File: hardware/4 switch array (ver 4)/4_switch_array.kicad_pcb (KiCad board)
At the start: 2 copper layers, 45.5 x 48.5 mm, 24 parts, among them J1 Conn_01x04, J2 Conn_01x04, J3 Conn_01x02, J4 Conn_01x02, J5 Conn_01x02, J6 Conn_01x02, J7 Conn_01x02, J8 Conn_01x02, Q1 Q_NPN_EBC, Q2 Q_NPN_EBC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

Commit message: Add high power switch and change 4 switch array
- added high power switch
- removed shift register from 4 switch array
- changed some references on silk layer
- small changes in switch arrays' tracing (width and paths)
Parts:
- removed C1: 100nF, Capacitor_THT:C_Disc_D7.0mm_W2.5mm_P5.00mm
- removed U1: 74HC595, Package_DIP:DIP-16_W7.62mm
- moved REF** 16.9 mm to (147.0, 51.0)
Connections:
- J1 pad 1: SER_IN -> OUT_1
- J1 pad 2: RCLK -> OUT_0
- J1 pad 3: +5V -> Net-(J1-Pad3)
- J2 pad 1: SRCLK -> OUT_2
- J2 pad 2: SRCLR -> OUT_3
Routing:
- net +5V: track 26.7 -> 0.00 mm
- net SER_IN: track 14.8 -> 0.00 mm
- net RCLK: track 13.3 -> 0.00 mm
- net OUT_0: track 5.62 -> 17.3 mm
- net OUT_2: track 7.88 -> 19.3 mm
- net SRCLR: track 9.19 -> 0.00 mm
- net SRCLK: track 9.17 -> 0.00 mm
- net OUT_3: track 17.6 -> 20.6 mm
- net OUT_1: track 15.6 -> 18.5 mm
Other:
- board text removed: "OUT0"
- board text removed: "OUT1"
- board text removed: "OUT2"
- board text removed: "OUT3"
- board text removed: "RCLK"
- board text removed: "SER_IN"
- board text removed: "SRCLK"
- board text removed: "VCC"
- board text removed: "~SRCLR~"

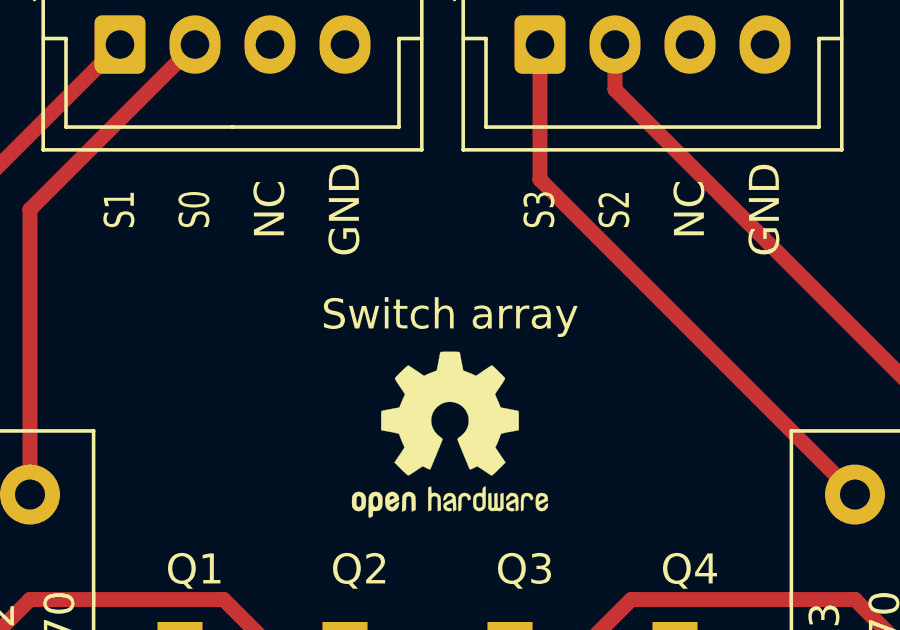
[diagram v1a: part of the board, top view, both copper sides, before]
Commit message: Add version number to boards
Add version number to boards and update screenshots, zip gerber archives
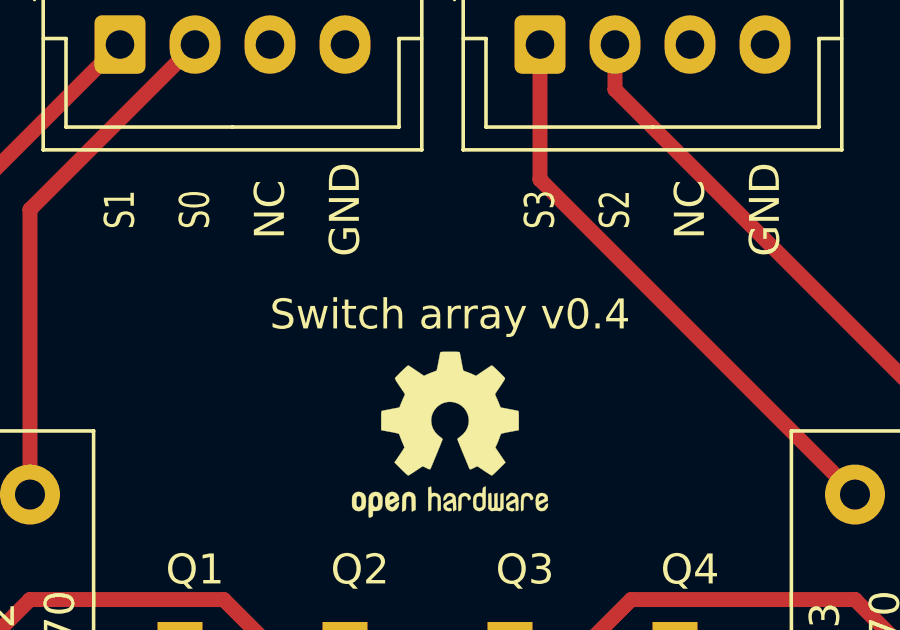
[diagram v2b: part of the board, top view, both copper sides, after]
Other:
- board text added: "Switch array v0.4"
- board text removed: "Switch array"
